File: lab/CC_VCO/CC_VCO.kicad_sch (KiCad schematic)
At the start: 15 parts, among them Q1 BS170, Q2 BS170

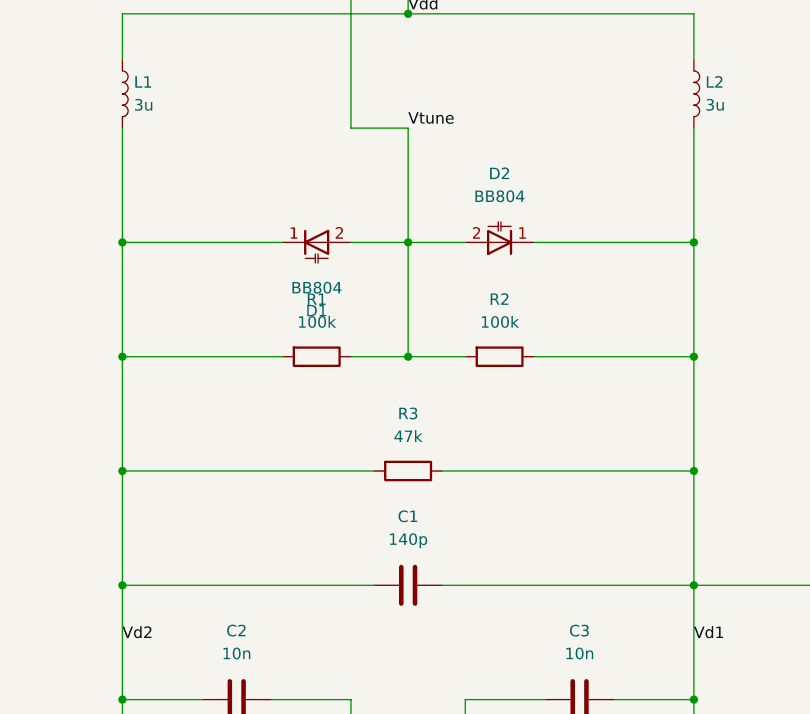
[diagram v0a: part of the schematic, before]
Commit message: CC-VCO Schematic und Quarto doku angepasst
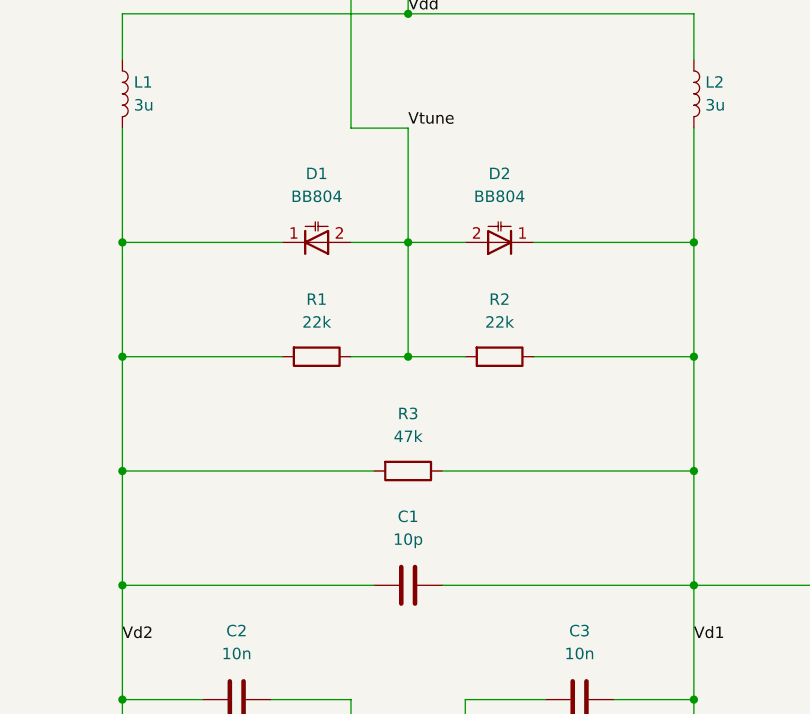
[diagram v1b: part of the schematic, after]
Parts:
- C1: value 140p -> 10p
- R1, R2: value 100k -> 22k
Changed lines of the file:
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@@
 			)
 		)
-		(property "Value" "140p"
+		(property "Value" "10p"
 			(at 133.35 109.22 90)
 			(show_name no)
@@
 			)
 		)
-		(property "Value" "100k"
+		(property "Value" "22k"
 			(at 123.19 85.09 90)
 			(show_name no)
@@
 			)
 		)
-		(property "Value" "100k"
+		(property "Value" "22k"
 			(at 143.51 85.09 90)
 			(show_name no)
@@
 		(lib_id "Device:D_Capacitance")
 		(at 123.19 76.2 0)
+		(mirror x)
 		(unit 1)
 		(body_style 1)
@@
 		(dnp no)
 		(property "Reference" "D1"
-			(at 123.19 83.82 0)
+			(at 123.19 68.58 0)
 			(show_name no)
 			(do_not_autoplace no)
@@
 		)
 		(property "Value" "BB804"
-			(at 123.19 81.28 0)
+			(at 123.19 71.12 0)
 			(show_name no)
 			(do_not_autoplace no)
@@
 			)
 		)
-		(property "Sim.Library" "C:\\Users\\mauri\\OneDrive\\Dokumente\\KiCad\\10.0\\symbols\\varactor.cir"
+		(property "Sim.Library" "varactor.cir"
 			(at 123.19 76.2 0)
 			(hide yes)
@@
 			)
 		)
-		(property "Sim.Library" "C:\\Users\\mauri\\OneDrive\\Dokumente\\KiCad\\10.0\\symbols\\varactor.cir"
+		(property "Sim.Library" "varactor.cir"
 			(at 143.51 76.2 0)
 			(hide yes)

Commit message: Bericht angepasst
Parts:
- D1, D2: value BB804 -> BB112
- L1, L2: value 3u -> 3.3u
- R1, R2: value 22k -> 10k
- R3: value 47k -> 1Meg
- R4: value 47k -> 25.5k
- Vtune1: value 1 -> 8
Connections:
- net Out: now also C1.2, C3.2, R2.2; no longer C1.1, C3.1, R2.1
- net Vd2: now also C1.1; no longer C1.2
- net Vtune: now also R2.1; no longer R2.2
- net at Q2.2 (G): now also C3.1; no longer C3.2
- net GND renamed 0

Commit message: Platine erstellt
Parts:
- L1, L2: value 3.3u -> 3u
- R3: value 1Meg -> 10k
- Vtune1: value 8 -> 1
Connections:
- net Out: now also C1.1, C3.1, R2.1; no longer C1.2, C3.2, R2.2
- net Vd2: now also C1.2; no longer C1.1
- net Vtune: now also R2.2; no longer R2.1
- net at Q2.2 (G): now also C3.2; no longer C3.1
- net 0 renamed GND

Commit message: Platine erstellt
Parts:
- C1, C2, C3: footprint (none) -> Capacitor_THT:C_Disc_D5.0mm_W2.5mm_P5.00mm
- D1, D2, Q1, Q2: footprint (none) -> Package_TO_SOT_THT:TO-92_Inline
- L1, L2: footprint (none) -> Inductor_THT:L_Axial_L9.5mm_D4.0mm_P15.24mm_Horizontal_Fastron_SMCC
- R1, R2, R3, R4: footprint (none) -> Resistor_THT:R_Axial_DIN0207_L6.3mm_D2.5mm_P7.62mm_Horizontal
- Vdd1, Vtune1: footprint (none) -> Connector_PinHeader_2.54mm:PinHeader_1x02_P2.54mm_Vertical
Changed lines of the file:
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@@
 			)
 		)
-		(property "Footprint" ""
+		(property "Footprint" "Package_TO_SOT_THT:TO-92_Inline"
 			(at 99.06 137.16 0)
 			(hide yes)
@@
 			)
 		)
-		(property "Footprint" ""
+		(property "Footprint" "Capacitor_THT:C_Disc_D5.0mm_W2.5mm_P5.00mm"
 			(at 110.49 127.9652 0)
 			(hide yes)
@@
 			)
 		)
-		(property "Footprint" ""
+		(property "Footprint" "Package_TO_SOT_THT:TO-92_Inline"
 			(at 167.64 137.16 0)
 			(hide yes)
@@
 			)
 		)
-		(property "Footprint" ""
+		(property "Footprint" "Capacitor_THT:C_Disc_D5.0mm_W2.5mm_P5.00mm"
 			(at 148.59 127.9652 0)
 			(hide yes)
@@
 			)
 		)
-		(property "Footprint" ""
+		(property "Footprint" "Resistor_THT:R_Axial_DIN0207_L6.3mm_D2.5mm_P7.62mm_Horizontal"
 			(at 131.572 161.29 90)
 			(hide yes)
@@
 			)
 		)
-		(property "Footprint" ""
+		(property "Footprint" "Capacitor_THT:C_Disc_D5.0mm_W2.5mm_P5.00mm"
 			(at 129.54 115.2652 0)
 			(hide yes)
@@
 			)
 		)
-		(property "Footprint" ""
+		(property "Footprint" "Resistor_THT:R_Axial_DIN0207_L6.3mm_D2.5mm_P7.62mm_Horizontal"
 			(at 123.19 87.122 90)
 			(hide yes)
@@
 			)
 		)
-		(property "Footprint" ""
+		(property "Footprint" "Resistor_THT:R_Axial_DIN0207_L6.3mm_D2.5mm_P7.62mm_Horizontal"
 			(at 133.35 99.822 90)
 			(hide yes)
@@
 			)
 		)
-		(property "Footprint" ""
+		(property "Footprint" "Connector_PinHeader_2.54mm:PinHeader_1x02_P2.54mm_Vertical"
 			(at 76.2 55.88 0)
 			(hide yes)
@@
 			)
 		)
-		(property "Footprint" ""
+		(property "Footprint" "Inductor_THT:L_Axial_L9.5mm_D4.0mm_P15.24mm_Horizontal_Fastron_SMCC"
 			(at 165.1 59.69 0)
 			(hide yes)
@@
 			)
 		)
-		(property "Footprint" ""
+		(property "Footprint" "Resistor_THT:R_Axial_DIN0207_L6.3mm_D2.5mm_P7.62mm_Horizontal"
 			(at 143.51 87.122 90)
 			(hide yes)
@@
 			)
 		)
-		(property "Footprint" ""
+		(property "Footprint" "Package_TO_SOT_THT:TO-92_Inline"
 			(at 123.19 76.2 0)
 			(hide yes)
@@
 			)
 		)
-		(property "Footprint" ""
+		(property "Footprint" "Inductor_THT:L_Axial_L9.5mm_D4.0mm_P15.24mm_Horizontal_Fastron_SMCC"
 			(at 101.6 59.69 0)
 			(hide yes)
@@
 			)
 		)
-		(property "Footprint" ""
+		(property "Footprint" "Connector_PinHeader_2.54mm:PinHeader_1x02_P2.54mm_Vertical"
 			(at 190.5 55.88 0)
 			(hide yes)
@@
 			)
 		)
-		(property "Footprint" ""
+		(property "Footprint" "Package_TO_SOT_THT:TO-92_Inline"
 			(at 143.51 76.2 0)
 			(hide yes)

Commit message: Platine aktualisiert
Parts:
- removed C2, C3: 10n, Capacitor_THT:C_Disc_D5.0mm_W2.5mm_P5.00mm, symbol Device:C
- added J1: Conn_Coaxial, Connector_Coaxial:BNC_Amphenol_031-5539_Vertical, symbol Connector:Conn_Coaxial
- L1, L2: value 3u -> 3,3u
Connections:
- net GND: now also J1.2 (Ext)
- net Out: now also Q2.2 (G)
- net Vd2: now also Q1.2 (G)
- net Vtune: now also J1.1 (In)

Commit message: Schematic update
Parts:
- removed J1: Conn_Coaxial, Connector_Coaxial:BNC_Amphenol_031-5539_Vertical, symbol Connector:Conn_Coaxial
- added C2, C3: 10n, symbol Device:C
- C1: footprint Capacitor_THT:C_Disc_D5.0mm_W2.5mm_P5.00mm -> (none)
- D1, D2, Q1, Q2: footprint Package_TO_SOT_THT:TO-92_Inline -> (none)
- L1, L2: value 3,3u -> 3.3u; footprint Inductor_THT:L_Axial_L9.5mm_D4.0mm_P15.24mm_Horizontal_Fastron_SMCC -> (none)
- R1, R2, R3, R4: footprint Resistor_THT:R_Axial_DIN0207_L6.3mm_D2.5mm_P7.62mm_Horizontal -> (none)
- Vdd1: footprint Connector_PinHeader_2.54mm:PinHeader_1x02_P2.54mm_Vertical -> (none)
- Vtune1: value 1 -> 8; footprint Connector_PinHeader_2.54mm:PinHeader_1x02_P2.54mm_Vertical -> (none)
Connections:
- net Out: now also C3.1; no longer Q2.2 (G)
- net Vd2: now also C2.2; no longer Q1.2 (G)
- new net: C3.2, Q2.2 (G)
- new net: C2.1, Q1.2 (G)
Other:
- moved on the sheet: C1, D1, D2, L1, L2, Q1, Q2, R1, R2, R3, R4, Vdd1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
